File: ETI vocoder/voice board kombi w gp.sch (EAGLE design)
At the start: 170 parts, among them IC1 TL072P, IC1. TL072P, IC2 TL072P, IC2. TL072P, IC3 TL081P, IC3. TL081P, IC4 TL081P, IC4. TL081P, IC5 TL072P, IC6 LM13600AN, IC7 TL072P, IC7. TL072P, P1. C-OR-R050_075-030X100, P10. C-OR-R050_075-030X100, P13. C-OR-R050_075-030X100, P14. C-OR-R050_075-030X100, P16 C-OR-R050_075-030X100, P2. C-OR-R050_075-030X100, P5. C-OR-R050_075-030X100, P6. C-OR-R050_075-030X100, P8 C-OR-R050_075-030X100, P9. C-OR-R050_075-030X100, Q1 BF244C, Q1. BF244C, Q2 BC212L, Q2. BC212L

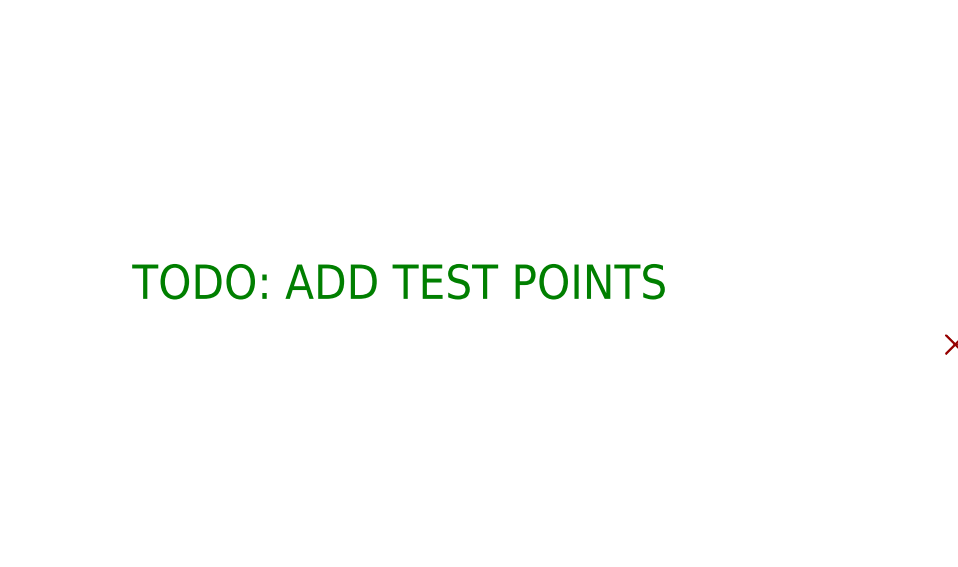
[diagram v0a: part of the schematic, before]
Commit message: Updated trimpot names and positions
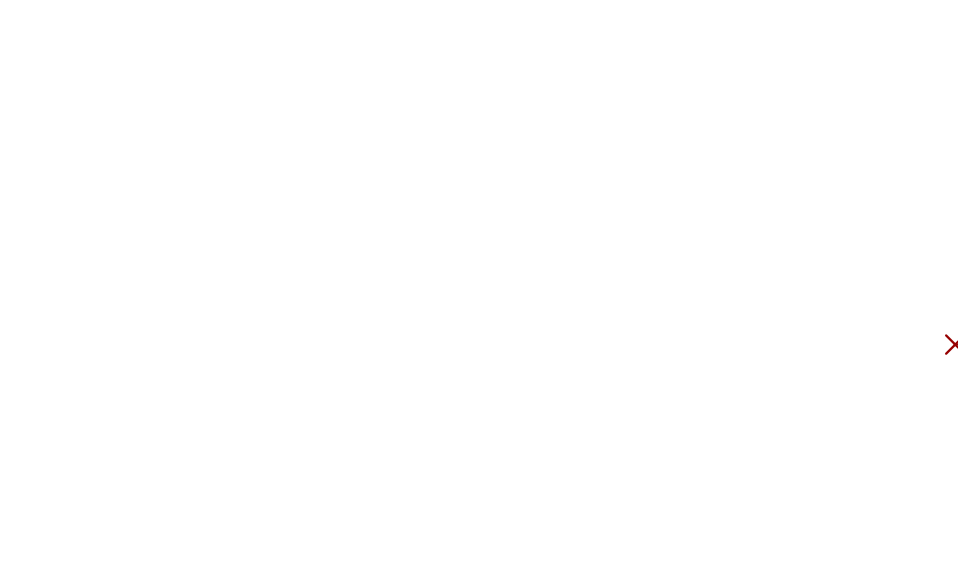
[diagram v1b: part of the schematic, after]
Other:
- note removed: "TODO: ADD TEST POINTS"
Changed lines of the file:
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@@
 <text x="89.154" y="130.81" size="1.016" layer="97" rot="R180">L: R22
 B: N/C</text>
-<text x="-58.42" y="144.78" size="3.81" layer="91">TODO: ADD TEST POINTS</text>
 </plain>
 <instances>

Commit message: Updated trimpot names and positions
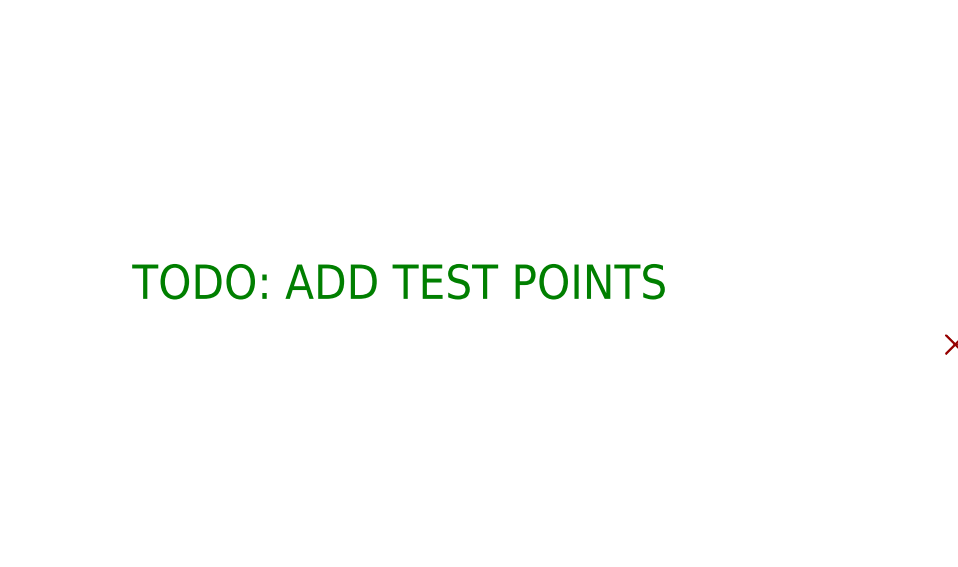
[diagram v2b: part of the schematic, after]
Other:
- note added: "TODO: ADD TEST POINTS"
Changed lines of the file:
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@@
 <text x="89.154" y="130.81" size="1.016" layer="97" rot="R180">L: R22
 B: N/C</text>
+<text x="-58.42" y="144.78" size="3.81" layer="91">TODO: ADD TEST POINTS</text>
 </plain>
 <instances>
